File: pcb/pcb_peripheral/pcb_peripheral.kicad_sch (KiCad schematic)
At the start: 23 parts, among them J1 Pump 1, J2 Pump 2

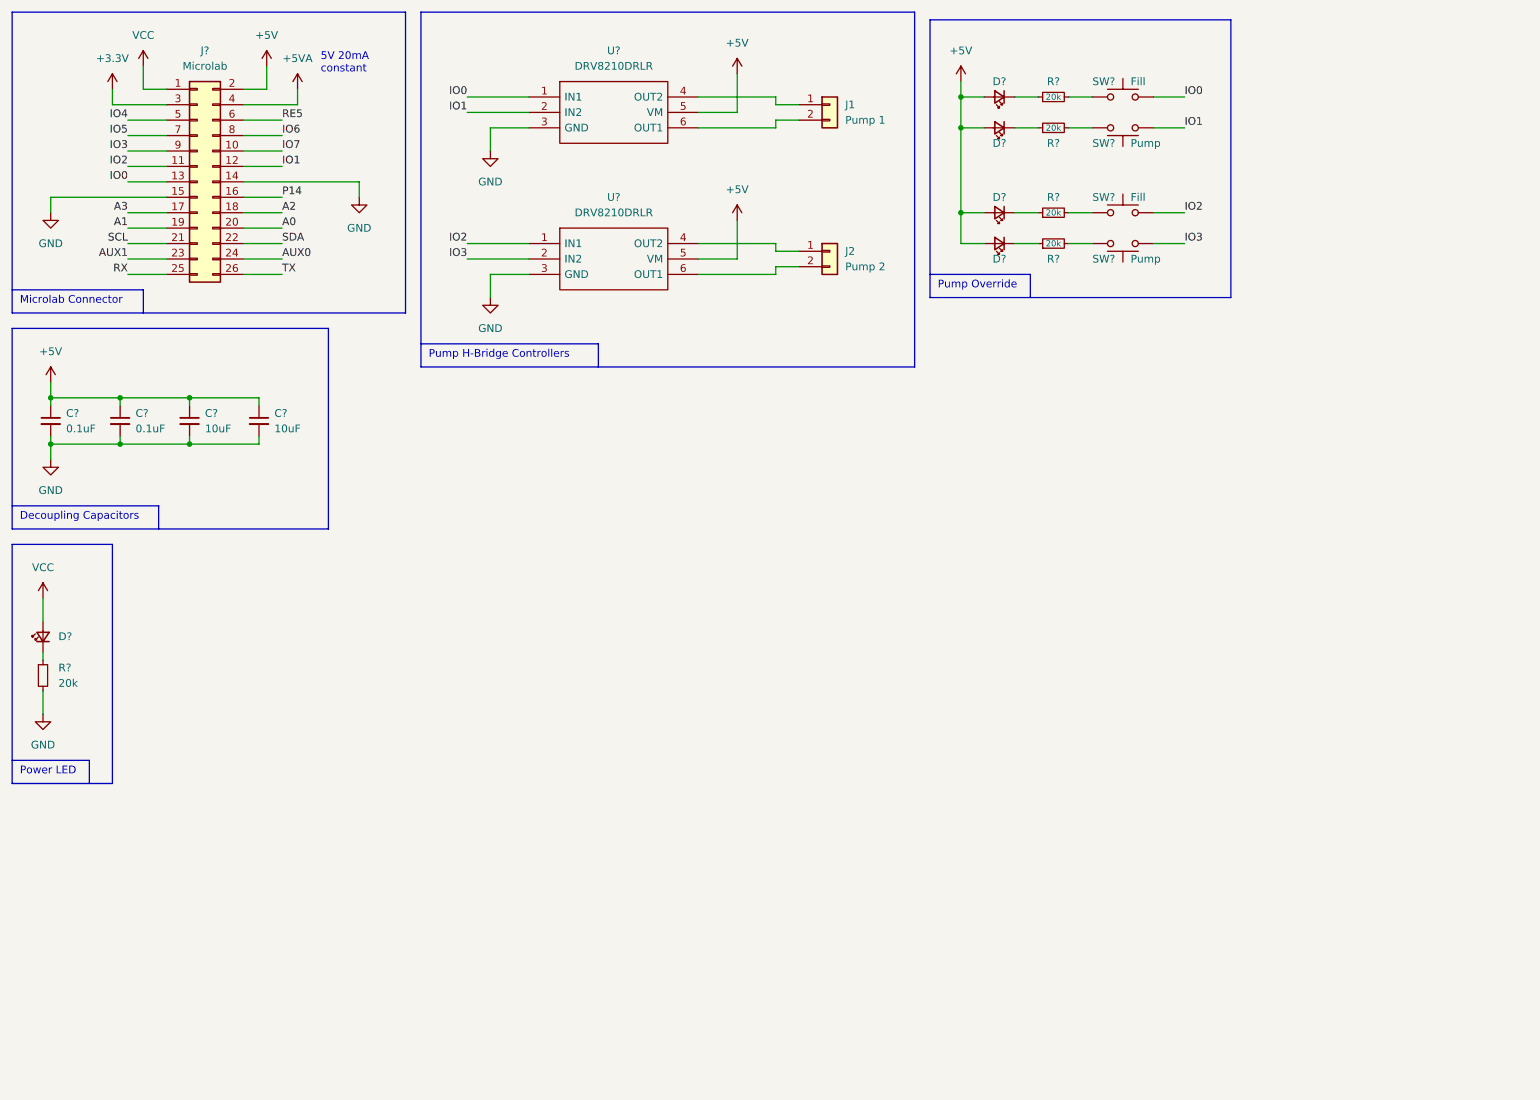
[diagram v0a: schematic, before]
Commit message: schematic v0.1
completed circuitry on schematic:
- pump h-bridge control
- chamber LED nmos low side switch
- arduino O2 sensor connector
- debug LEDs and buttons

todo:
- assign footprints
- build board
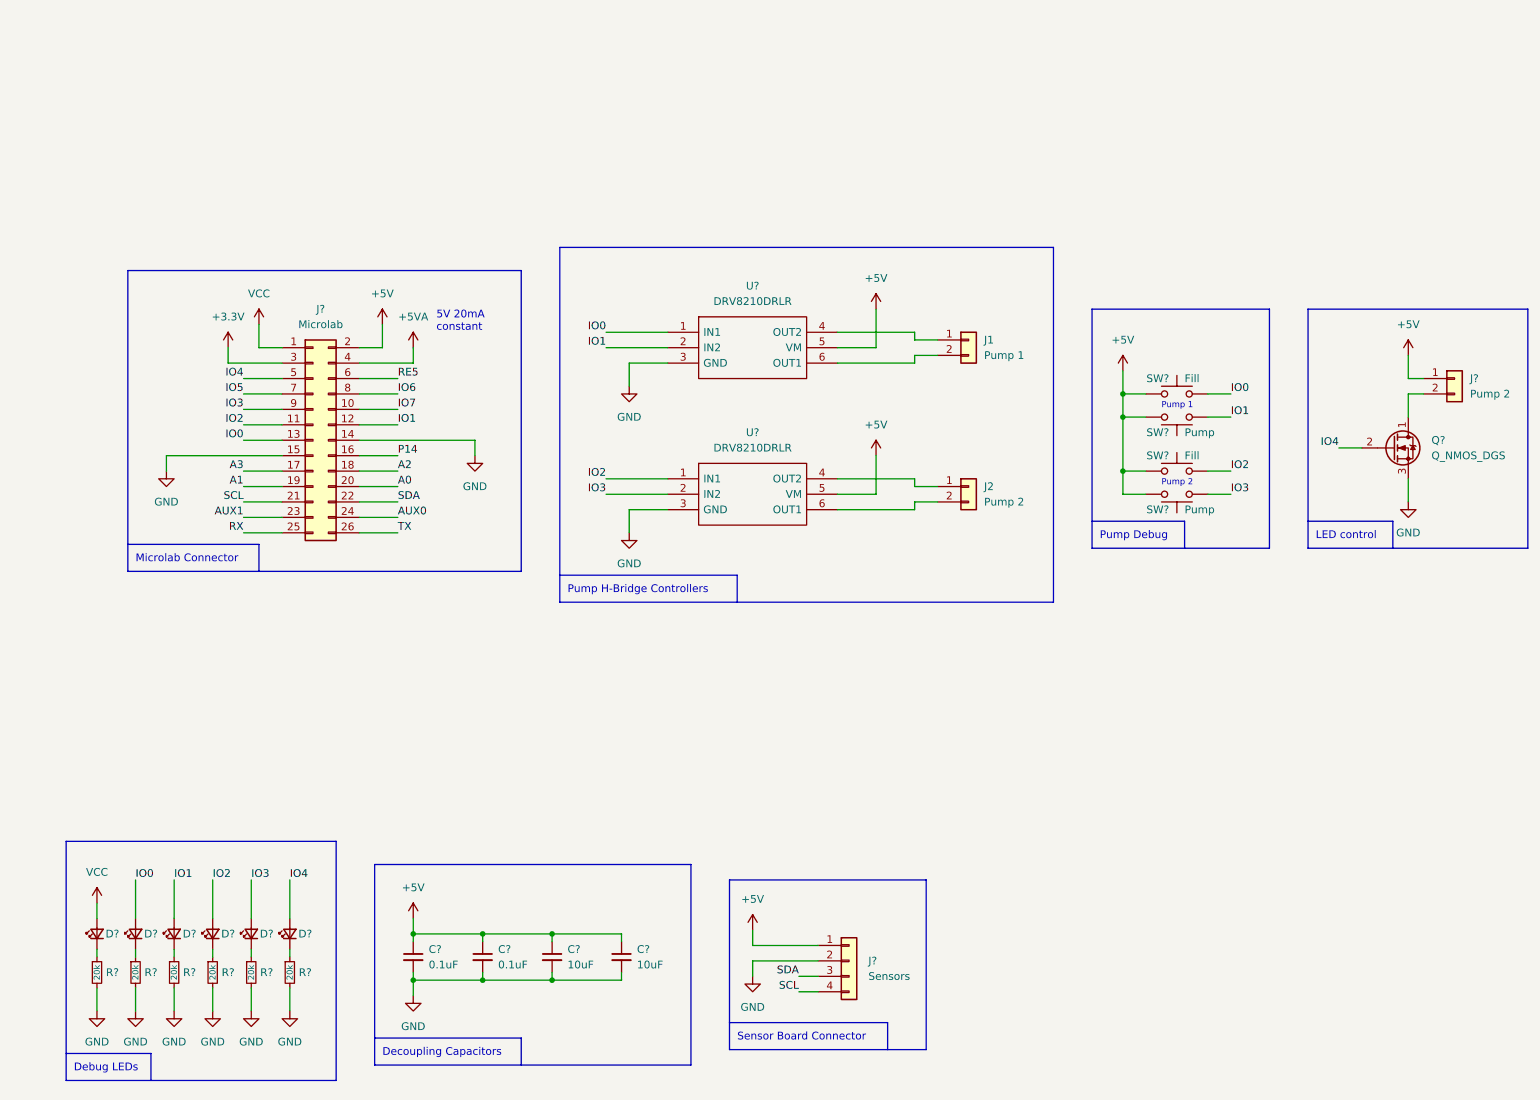
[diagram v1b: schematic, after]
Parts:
- removed D? (x4): APHHS1005LSECK/J3-PF, symbol Device:LED_Small
- removed R? (x4): 20k, symbol Device:R_Small
- removed SW? (x2): Pump, symbol Switch:SW_Push
- removed SW? (x2): Fill, symbol Switch:SW_Push
- added D? (x5): APHHS1005LSECK/J3-PF, symbol Device:LED_Small
- added J?: Sensors, symbol Connector_Generic:Conn_01x04
- added J?: Pump 2, symbol Connector_Generic:Conn_01x02
- added Q?: Q_NMOS_DGS, symbol Device:Q_NMOS_DGS
- added R? (x5): 20k, symbol Device:R_Small
- added SW? (x2): Pump, symbol Switch:SW_Push
- added SW? (x2): Fill, symbol Switch:SW_Push
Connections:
- net +5V: now also J?.1 (Pin_1), J?.1 (Pin_1), SW?.1, SW?.1, SW?.2, SW?.2; no longer D?.2 (A)
- net GND: now also R?.2, J?.2 (Pin_2), Q?.3 (S), R?.2, R?.2, R?.2, R?.2, R?.2
- net IO0: now also D?.2 (A), SW?.2
- net IO1: now also D?.2 (A), SW?.1
- net IO2: now also D?.2 (A), SW?.2
- net IO3: now also D?.2 (A), SW?.1
- net IO4: now also D?.2 (A), Q?.2 (G)
- net SCL: now also J?.4 (Pin_4)
- net SDA: now also J?.3 (Pin_3)
- net VCC: now also D?.2 (A)
- new net: D?.1 (K), R?.1 (x5)
- new net: J?.2 (Pin_2), Q?.1 (D)
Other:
- note added: "Debug LEDs"
- note added: "LED control"
- note added: "Pump 1"
- note added: "Pump 2"
- note added: "Pump Debug"
- note added: "Sensor Board Connector"
- note removed: "Power LED"
- note removed: "Pump Override"
- moved on the sheet: C?, D?, J1, J2, J?, R?, U?

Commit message: updated schematic footprints
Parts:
- added H1, H2, H3, H4: M2, MountingHole:MountingHole_2.2mm_M2_DIN965_Pad, symbol Mechanical:MountingHole_Pad
- C1, C2, C3, C4: renamed from C?; footprint (none) -> Capacitor_SMD:C_0402_1005Metric_Pad0.74x0.62mm_HandSolder
- D1, D2, D3, D4, D5, D6: renamed from D?; footprint (none) -> LED_SMD:LED_0402_1005Metric_Pad0.77x0.64mm_HandSolder
- J1, J2: footprint (none) -> Connector_JST:JST_SH_BM02B-SRSS-TB_1x02-1MP_P1.00mm_Vertical
- J3: renamed from J?; footprint (none) -> Connector_PinSocket_2.00mm:PinSocket_2x13_P2.00mm_Vertical
- J4: renamed from J?; footprint (none) -> Connector_JST:JST_SH_BM04B-SRSS-TB_1x04-1MP_P1.00mm_Vertical
- J5: renamed from J?; footprint (none) -> Connector_JST:JST_SH_BM02B-SRSS-TB_1x02-1MP_P1.00mm_Vertical
- Q1: renamed from Q?; footprint (none) -> Package_TO_SOT_SMD:SOT-23
- R1, R2, R3, R4, R5, R6: renamed from R?; footprint (none) -> Resistor_SMD:R_0402_1005Metric_Pad0.72x0.64mm_HandSolder
- SW1, SW2, SW3, SW4: renamed from SW?; footprint (none) -> Button_Switch_SMD:SW_SPST_B3U-3000P
- U1, U2: renamed from U?; footprint SOTFL50P160X60-6N -> Mouser:SOTFL50P160X60-6N
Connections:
- net GND: now also H1.1, H2.1, H3.1, H4.1
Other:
- note added: "Mounting Holes"
- moved on the sheet: C1, C2, C3, C4, D1, D2, D3, D4, D5, D6, J4, R1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

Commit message: inter-component routing finished
placed and routed all components except IO connections
don't have access to the internet to check the placement of the microlab header therefore no IO routing
might change the placement of the pump, led, and sensor headers when I get internet access
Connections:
- net +5V: now also SW2.1, SW4.1; no longer SW2.2, SW4.2
- net IO1: now also SW2.2; no longer SW2.1
- net IO3: now also SW4.2; no longer SW4.1
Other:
- moved on the sheet: SW2, SW4
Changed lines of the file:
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@@
     (pin "2")
   )
-  (symbol (lib_id "Switch:SW_Push") (at 205.74 93.345 180) (unit 1)
+  (symbol (lib_id "Switch:SW_Push") (at 205.74 93.345 0) (mirror x) (unit 1)
     (in_bom yes) (on_board yes)
     (property "Reference" "SW4" (id 0) (at 204.47 95.885 0)
-      (effects (font (size 1.27 1.27)) (justify left))
+      (effects (font (size 1.27 1.27)) (justify right))
     )
     (property "Value" "Pump" (id 1) (at 207.01 95.885 0)
-      (effects (font (size 1.27 1.27)) (justify right))
+      (effects (font (size 1.27 1.27)) (justify left))
     )
     (property "Footprint" "Button_Switch_SMD:SW_SPST_B3U-3000P" (id 2) (at 205.74 98.425 0)
@@
     (pin "4")
   )
-  (symbol (lib_id "Switch:SW_Push") (at 205.74 80.645 180) (unit 1)
+  (symbol (lib_id "Switch:SW_Push") (at 205.74 80.645 0) (mirror x) (unit 1)
     (in_bom yes) (on_board yes)
     (property "Reference" "SW2" (id 0) (at 204.47 83.185 0)
+      (effects (font (size 1.27 1.27)) (justify right))
+    )
+    (property "Value" "Pump" (id 1) (at 207.01 83.185 0)
       (effects (font (size 1.27 1.27)) (justify left))
     )
-    (property "Value" "Pump" (id 1) (at 207.01 83.185 0)
-      (effects (font (size 1.27 1.27)) (justify right))
-    )
     (property "Footprint" "Button_Switch_SMD:SW_SPST_B3U-3000P" (id 2) (at 205.74 85.725 0)
